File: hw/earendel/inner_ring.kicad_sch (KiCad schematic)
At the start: 40 parts, among them U2 IS31FL3236A-TQ

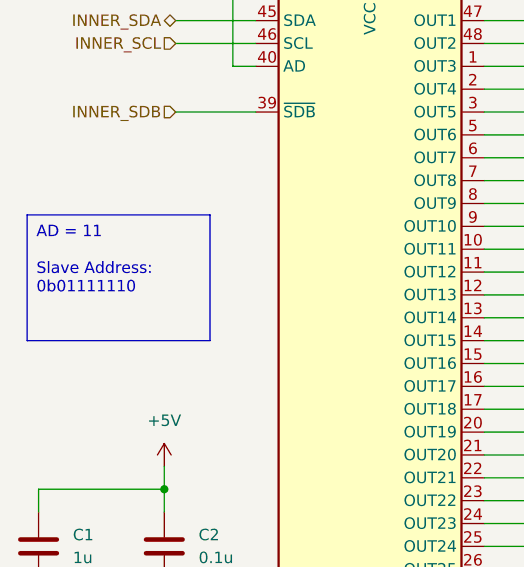
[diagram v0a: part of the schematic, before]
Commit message: Added MCU decoupling caps, started power
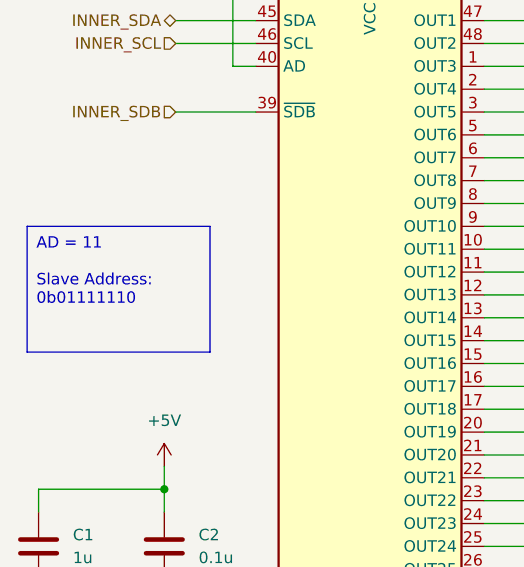
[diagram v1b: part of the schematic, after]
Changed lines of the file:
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@@
 	(text_box "AD = 11\n\nSlave Address: 0b01111110"
 		(exclude_from_sim no)
-		(at 50.8 68.58 0)
+		(at 50.8 69.85 0)
 		(size 20.32 13.97)
 		(stroke
